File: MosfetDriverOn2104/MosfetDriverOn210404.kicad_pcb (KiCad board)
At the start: 2 copper layers, 99.9 x 99.9 mm, 91 parts, among them J1 I2C HDR, J10 ENCODER HDR, J11 CROSS CONN, J12 motor, J13 Conn_01x02_Female, J2 AVR-ISP-6, J3 I2C HDR, J4 Screw_Terminal_01x02, J5 I2C HDR, J6 UART HDR, J7 5V HDR, J8 GND HDR, J9 servo hdr, Q1 IRF540N, Q2 IRF540N, Q3 IRF540N, Q4 IRF540N, SW1 SW_Push, SW2 SW_DIP_x04, SW3 SW_Push, SW4 SW_Push, U1 LM2576HVS-ADJ, U2 L7805, U3 IR2104, U4 LM358, U5 IR2104, U6 ATmega328P-AU-MCU_Microchip_A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

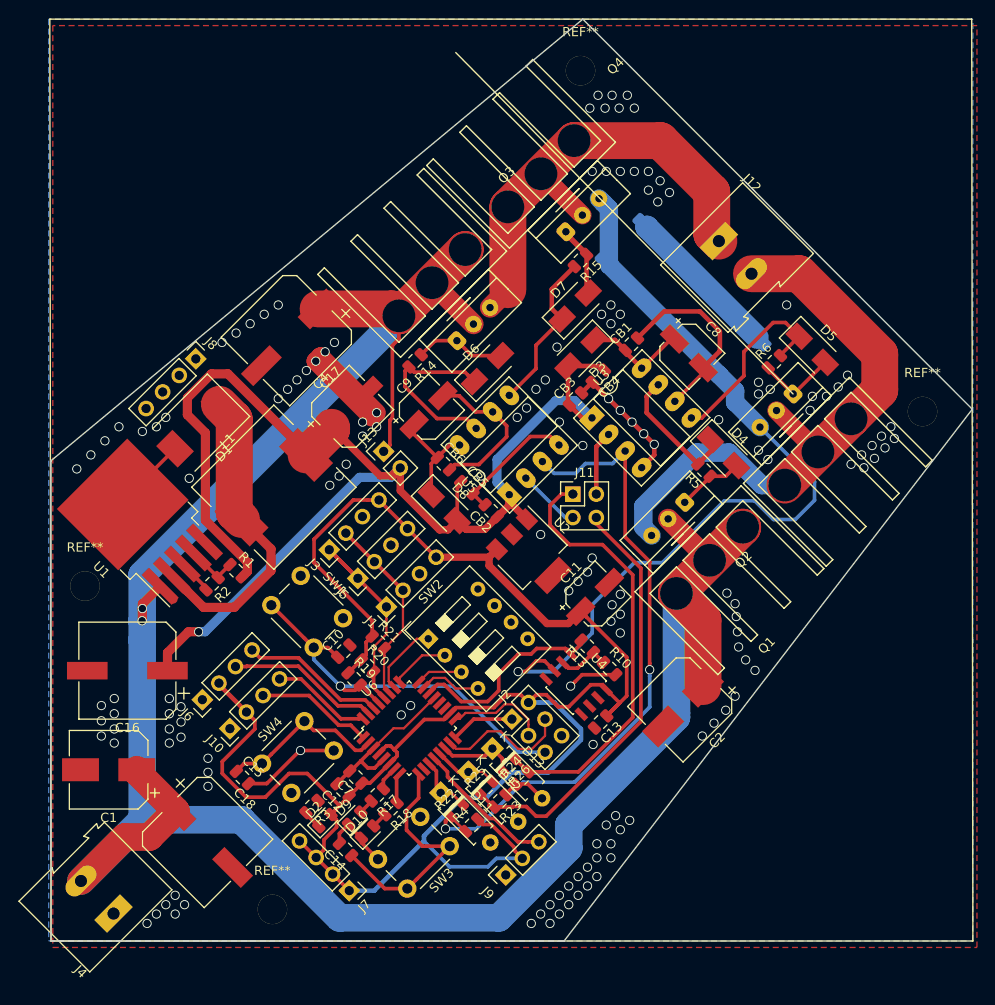
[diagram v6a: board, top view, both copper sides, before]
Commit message: #14 resolved
vcc stiching done.
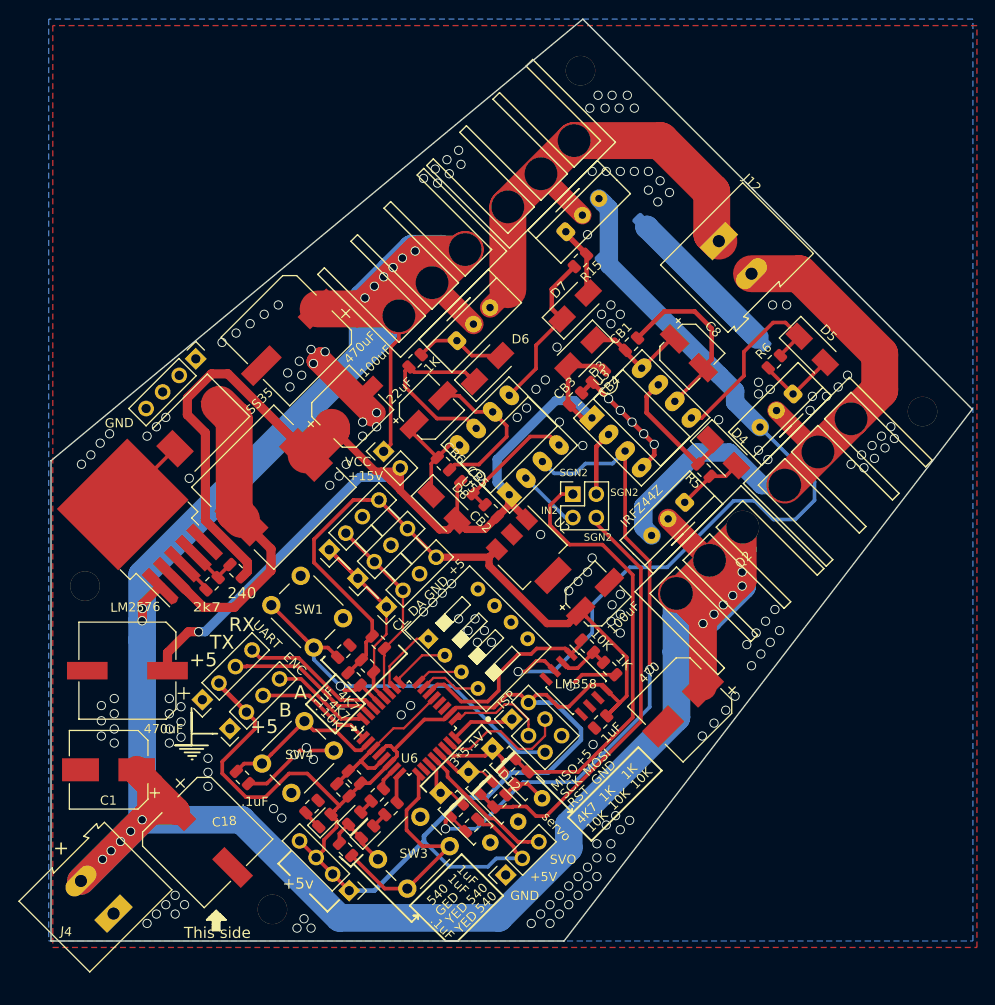
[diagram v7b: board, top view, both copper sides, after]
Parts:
- removed C16: 470, Capacitor_SMD:CP_Elec_10x7.9
- removed C7: C, Capacitor_SMD:C_0805_2012Metric
- removed R24: 10K, Resistor_SMD:R_0805_2012Metric
- added 10K: 10K, Resistor_SMD:R_0805_2012Metric, F.Cu at (156.0, 133.6)
- added 1uF: C, Capacitor_SMD:C_0805_2012Metric, F.Cu at (137.8, 133.5)
- added 470uF: 470, Capacitor_SMD:CP_Elec_10x7.9, F.Cu at (113.2, 121.9)
- C10, C14: value C_Small -> .1uF
- C12: value C_Small -> 1uF
- D1: value SS24 -> SS35
- D11: value 5.1V -> 3*5.1V
- D2: value POWER_LED -> GED
- J10: value ENCODER HDR -> ENC
- J6: value UART HDR -> UART
- J8: value GND HDR -> GND
- J9: value servo hdr -> servo
- YED: renamed from D9; value LED -> YED
- renumbered C15 to .1uF, C4 to 100uF, C11 to 100uF, R4 to 10K, R23 to 10K, R10 to 1K, R14 to 1K, R26 to 1K, R25 to 1K, C13 to 1uF, C9 to 22uF, C17 to 470uF, R22 to 4K7, Q1 to IRFZ44Z, J2 to ISP, U1 to LM2576, U4 to LM358
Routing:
- net VCC: track 256.9 -> 395.5 mm, vias 2 -> 19
- net /M2: track 51.1 -> 61.3 mm
- net +15V: track 146.2 -> 151.7 mm
- net /M1: track 79.6 -> 84.7 mm
- net Net-(C8-Pad2): track 20.6 -> 19.6 mm
- net GND: vias 153 -> 178
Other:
- board text added: "+"
- board text added: "+15V"
- board text added: "+5"
- board text added: "+5V"
- board text added: "+5v"
- board text added: "240"
- board text added: "2k7"
- board text added: "A"
- board text added: "B"
- board text added: "CL"
- board text added: "DA"
- board text added: "GND"
- board text added: "IN2"
- board text added: "MISO"
- board text added: "MOSI"
- board text added: "RST"
- board text added: "RX"
- board text added: "SCK"
- board text added: "SGN2"
- board text added: "SVO"
- board text added: "TX"
- board text added: "This side"
- board text added: "VCC"

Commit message: #16 #15 #14 #12
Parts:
- removed D6: D, Diode_SMD:D_SMA
- added SS27: D, Diode_SMD:D_SMA, F.Cu at (152.8, 88.6)
- 22uF: footprint Capacitor_SMD:CP_Elec_5x5.3 -> Capacitor_SMD:CP_Elec_6.3x5.7
- 22uF: renamed from C8; footprint Capacitor_SMD:CP_Elec_5x5.3 -> Capacitor_SMD:CP_Elec_6.3x5.7
- C1, C18: value 470 -> 470uF
- CB1: value .1 -> .1uF
- D3: value D -> SS27
- Q2, Q3, Q4: value IRF540N -> IRFZ44N
- R8: value 0E05 -> 5*0E05
- moved J8 1.55 mm to (119.7, 89.4), turned to 313 degrees
- moved J4 1.35 mm to (112.6, 147.3)
- moved 22uF 0.63 mm to (174.7, 87.7)
- moved 100uF 0.60 mm to (136.8, 93.2)
- moved C2 0.44 mm to (173.1, 126.1), turned to 231 degrees
- moved REF** 0.36 mm to (128.7, 147.6)
- moved 470uF 0.27 mm to (131.0, 85.9), turned to 220 degrees
- moved REF** 0.25 mm to (108.7, 113.0)
- renumbered R5 to 10, R6 to 10, 1K to 10, R15 to 10, IRFZ44Z to IRFZ44N, D4 to SS27, D5 to SS27, D7 to SS27
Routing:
- net /IS+: track 90.5 -> 79.3 mm
- net /M2: track 61.3 -> 51.0 mm
- net Net-(D6-Pad1): track 19.7 -> 21.1 mm
- net VCC: track 395.5 -> 394.2 mm, vias 19 -> 20
- net GND: vias 178 -> 189
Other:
- board size 99.9 x 99.9 mm -> 99.1 x 99.1 mm
- board text added: "I2C"
- board text added: "MI"
- board text added: "MO"
- board text removed: "MISO"
- board text removed: "MOSI"
- board text removed: "This side"
